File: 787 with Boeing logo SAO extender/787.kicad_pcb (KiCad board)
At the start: 2 copper layers, 94.7 x 100.3 mm, 3 parts

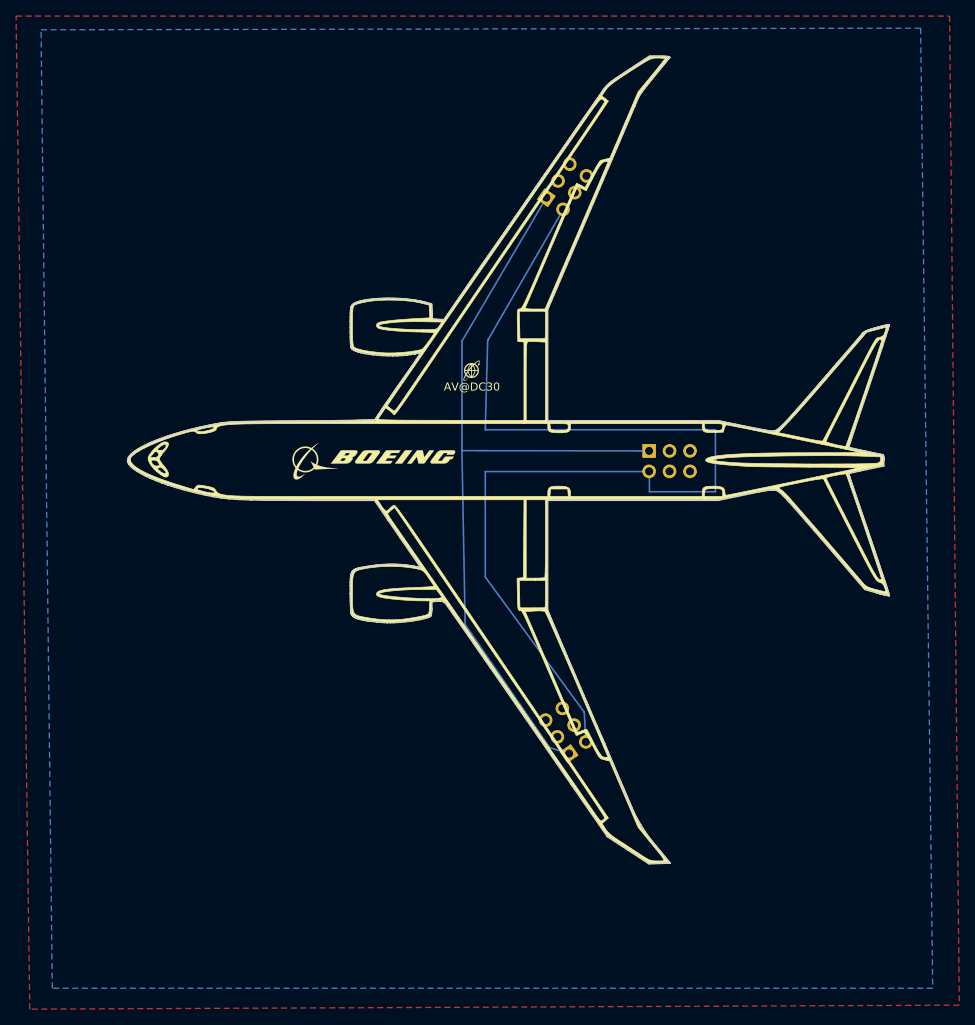
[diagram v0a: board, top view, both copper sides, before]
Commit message: Updated 787 SAO extender to have solder mask areas for the cockpit windows along with a rough outline of a keepout area.
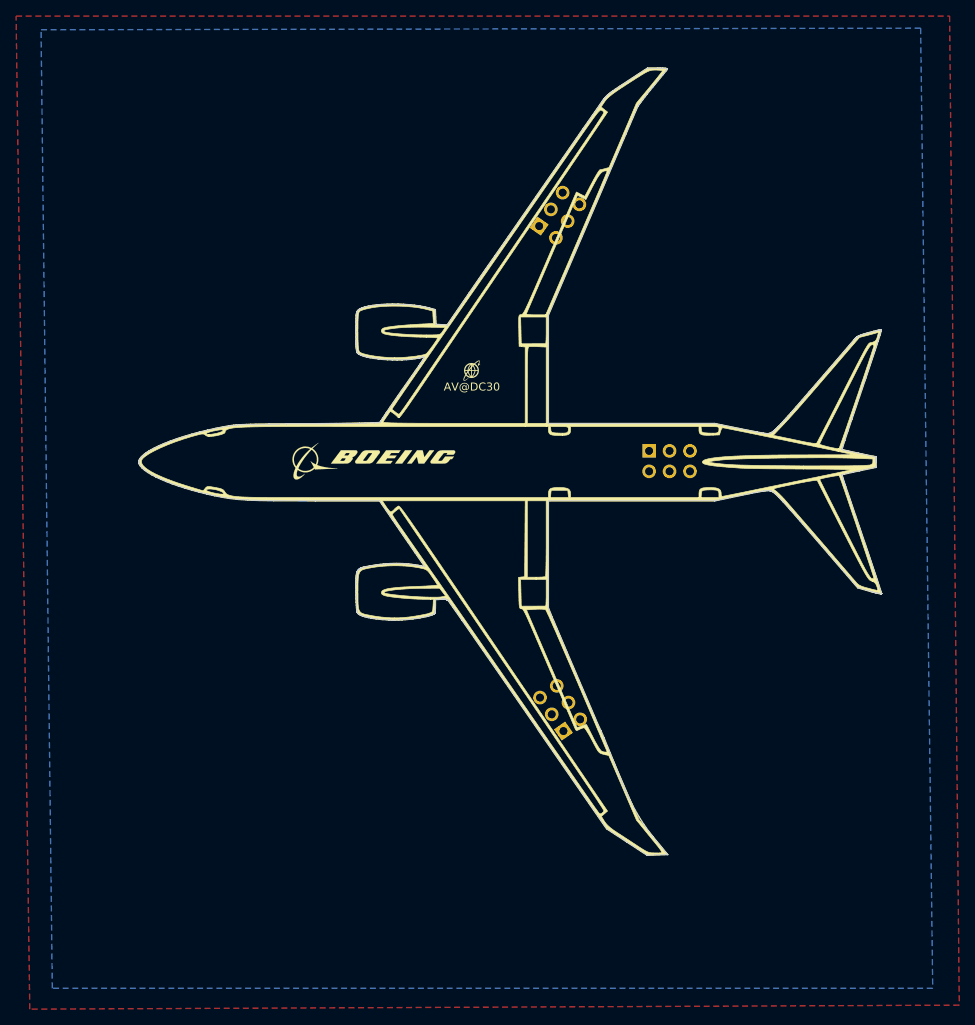
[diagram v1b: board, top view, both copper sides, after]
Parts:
- moved REF** 3.65 mm to (91.8, 85.5)
- moved REF** 2.89 mm to (94.8, 148.2)
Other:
- board size 94.7 x 100.3 mm -> 92.3 x 97.8 mm
- board text removed: "jlcjlcjlcjlc"

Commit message: Updates to 787 SAO extender
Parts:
- removed REF** (x3): PinHeader_2x03_P2.54mm_Vertical, Connector_PinHeader_2.54mm:PinHeader_2x03_P2.54mm_Vertical
- added D1: LED, sunled:XZMYK45WT-9, B.Cu at (46.9, 114.8)
- added J1: Conn_02x03_Counter_Clockwise, Connector_PinSocket_2.54mm:PinSocket_2x03_P2.54mm_Vertical, F.Cu at (105.6, 113.5)
- added J2: Conn_02x03_Counter_Clockwise, Connector_PinSocket_2.54mm:PinSocket_2x03_P2.54mm_Vertical, F.Cu at (91.6, 85.4)
- added J3: Conn_02x03_Counter_Clockwise, Connector_PinSocket_2.54mm:PinSocket_2x03_P2.54mm_Vertical, F.Cu at (94.4, 148.3)
- added R1: R, Resistor_SMD:R_1206_3216Metric, B.Cu at (53.5, 114.8)
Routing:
- net Net-(J1-Pin_5): track 0.00 -> 89.8 mm, vias 0 -> 2
- net Net-(J1-Pin_6): track 0.00 -> 85.0 mm, vias 0 -> 2
- net Net-(J1-Pin_3): track 0.00 -> 84.7 mm
- net Net-(J1-Pin_4): track 0.00 -> 79.2 mm
- net +3V3: track 0.00 -> 67.8 mm, vias 0 -> 2
- net GND: track 0.00 -> 16.7 mm, vias 0 -> 2
- net Net-(D1-A): track 0.00 -> 10.4 mm
- added copper zone on F.Cu, net +3V3
- added copper zone on B.Cu, net GND
- removed copper zone on B.Cu, net (none)
- removed copper zone on F.Cu, net (none)
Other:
- board text added: "jlcjlcjlcjlc"
- board text added: "v1"
